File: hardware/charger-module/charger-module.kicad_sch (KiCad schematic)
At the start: 72 parts, among them J1 Bus_PCI_Express_x1, J2 Conn_01x06_Pin, J3 RP_USB, J4 USB_C_Receptacle_USB2.0_14P, SW1 BOOT, SW2 RESET, U1 AMS1117-3.3, U2 W25Q32JVSSIQ, U3 RP2040, U4 MPQ4242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

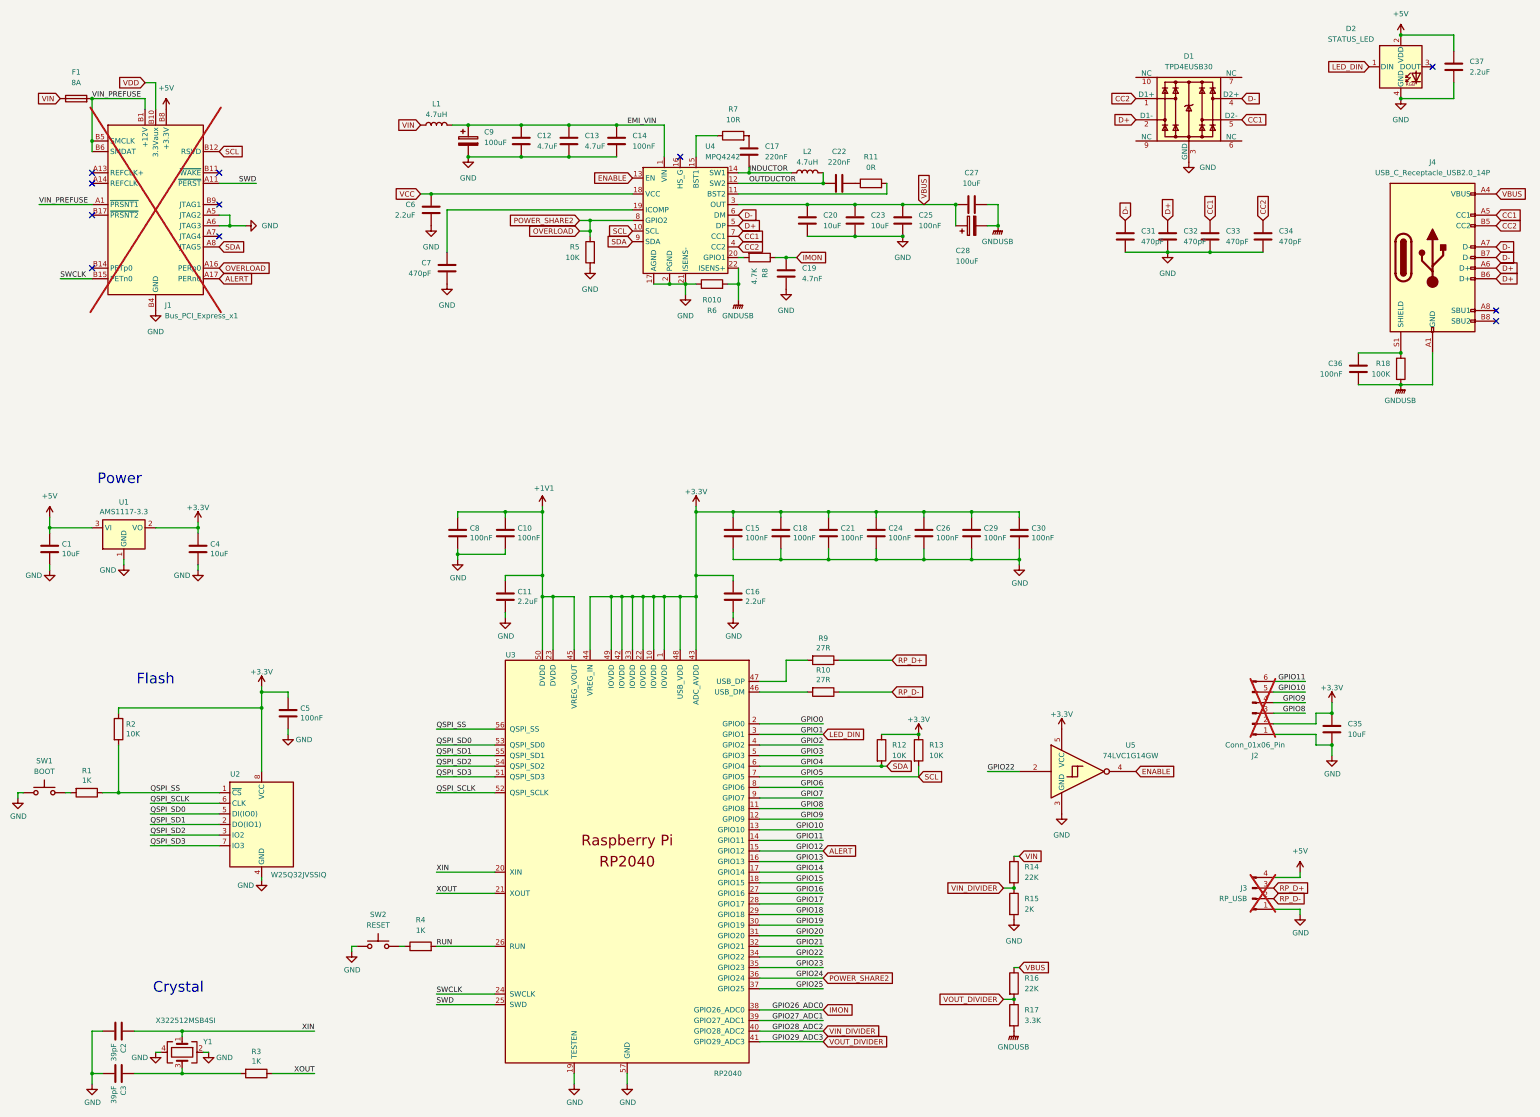
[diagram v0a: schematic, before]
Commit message: feat: split i2c network
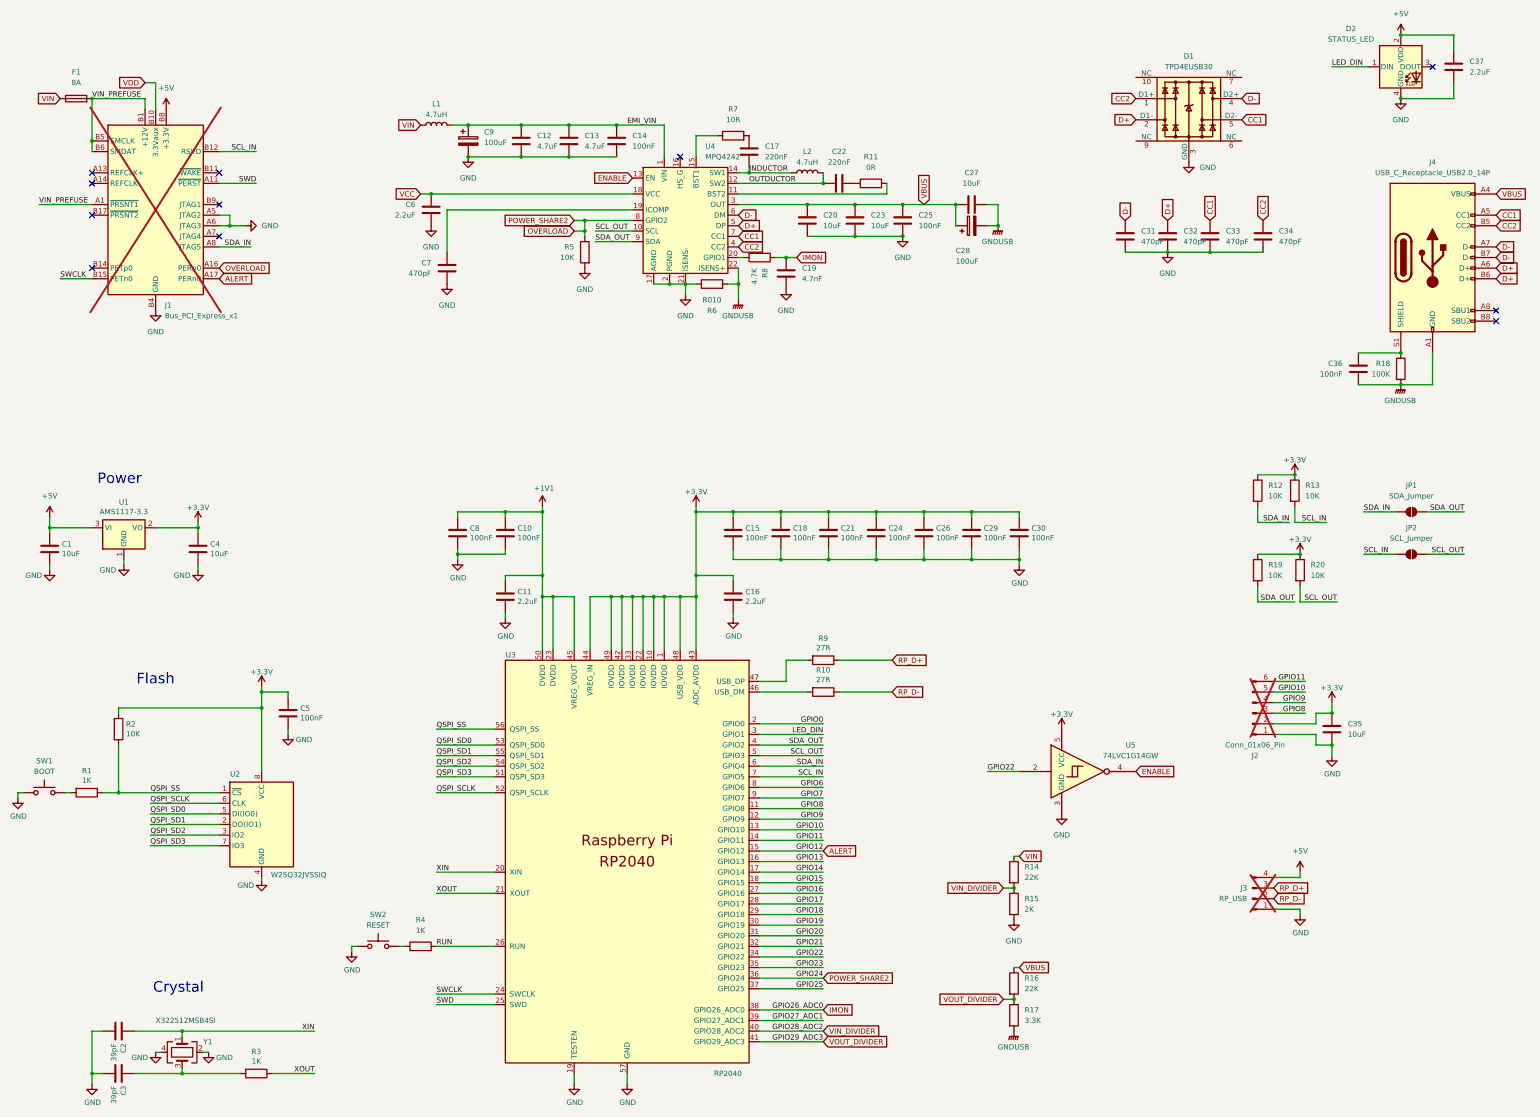
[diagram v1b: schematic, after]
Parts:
- added JP1: SDA_Jumper, Jumper:SolderJumper-2_P1.3mm_Open_TrianglePad1.0x1.5mm, symbol Jumper:SolderJumper_2_Open
- added JP2: SCL_Jumper, Jumper:SolderJumper-2_P1.3mm_Open_TrianglePad1.0x1.5mm, symbol Jumper:SolderJumper_2_Open
- added R19, R20: 10K, Resistor_SMD:R_0402_1005Metric, symbol Device:R
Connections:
- net +3.3V: now also R19.1, R20.1
- net GPIO2 renamed SDA_OUT
- net SDA_OUT: now also U4.9 (SDA), JP1.2 (B), R19.2
- net GPIO3 renamed SCL_OUT
- net SCL_OUT: now also U4.10 (SCL), JP2.2 (B), R20.2
- net SCL renamed SCL_IN
- net SCL_IN: now also JP2.1 (A); no longer U4.10 (SCL)
- net SDA renamed SDA_IN
- net SDA_IN: now also JP1.1 (A); no longer U4.9 (SDA)
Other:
- moved on the sheet: R5

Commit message: chore: switch jumper footprints
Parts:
- JP1, JP2: footprint Jumper:SolderJumper-2_P1.3mm_Open_TrianglePad1.0x1.5mm -> Jumper:SolderJumper-2_P1.3mm_Open_Pad1.0x1.5mm
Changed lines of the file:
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@@
 			)
 		)
-		(property "Footprint" "Jumper:SolderJumper-2_P1.3mm_Open_TrianglePad1.0x1.5mm"
+		(property "Footprint" "Jumper:SolderJumper-2_P1.3mm_Open_Pad1.0x1.5mm"
 			(at 372.11 135.89 0)
 			(effects
@@
 			)
 		)
-		(property "Footprint" "Jumper:SolderJumper-2_P1.3mm_Open_TrianglePad1.0x1.5mm"
+		(property "Footprint" "Jumper:SolderJumper-2_P1.3mm_Open_Pad1.0x1.5mm"
 			(at 372.11 146.05 0)
 			(effects

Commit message: fix: increase i2c pullup cap
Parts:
- C24: value 100nF -> 2.2uF; LCSC C1525 -> C12530
